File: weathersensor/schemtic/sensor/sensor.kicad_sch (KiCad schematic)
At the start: 18 parts, among them J1 Conn_Coaxial, J2 PS, J3 MS5611, J4 V_PANEL_IN, J5 V_PANEL_OUT, J6 V_BAT_IN, J7 V_BAT_OUT, U1 ESP32-DevKitC, U2 RFM95W-868S2

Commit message: Commit before fork
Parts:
- removed C1, C2: 100nF, Capacitor_THT:C_Disc_D3.0mm_W1.6mm_P2.50mm, symbol Device:C
- removed J2: PS, Connector_PinHeader_2.54mm:PinHeader_1x02_P2.54mm_Vertical, symbol Connector:Conn_01x02_Male
- removed J3: MS5611, Connector_PinHeader_2.54mm:PinHeader_1x07_P2.54mm_Vertical, symbol Connector:Conn_01x07_Female
- removed J5: V_PANEL_OUT, Connector_PinHeader_2.54mm:PinHeader_1x02_P2.54mm_Vertical, symbol Connector:Conn_01x02_Male
- removed J6: V_BAT_IN, TerminalBlock_RND:TerminalBlock_RND_205-00012_1x02_P5.00mm_Horizontal, symbol Connector:Screw_Terminal_01x02
- removed J7: V_BAT_OUT, Connector_PinHeader_2.54mm:PinHeader_1x02_P2.54mm_Vertical, symbol Connector:Conn_01x02_Male
- removed R2, R4: 510k, Resistor_THT:R_Axial_DIN0204_L3.6mm_D1.6mm_P5.08mm_Horizontal, symbol Device:R
- removed R3: 2.2M, Resistor_THT:R_Axial_DIN0204_L3.6mm_D1.6mm_P5.08mm_Horizontal, symbol Device:R
- removed U1: ESP32-DevKitC, ESP32-DEVKITC-32D:MODULE_ESP32-DEVKITC-32D, symbol Espressif:ESP32-DevKitC
- removed U2: RFM95W-868S2, RF_Module:HOPERF_RFM9XW_THT, symbol RF_Module:RFM95W-868S2
- removed U?: ESP32-WROOM, ESP32-footprints-Lib:ESP32, symbol ESP32-footprints-Shem-Lib:ESP32-WROOM
- added C3, C5, C6: 100u/16V, symbol Device:C_Polarized
- added C4: 100uF/100V, symbol Device:C_Polarized
- added J2: MS5611, Connector_PinHeader_2.54mm:PinHeader_1x07_P2.54mm_Vertical, symbol Connector:Conn_01x07_Female
- added J3: SWD, symbol Connector:Conn_01x04_Pin
- added J5: UART, symbol Connector:Conn_01x02_Pin
- added J7: BAT, Connector_JST:JST_EH_S2B-EH_1x02_P2.50mm_Horizontal, symbol Connector:Conn_01x02_Pin
- added SW1: SW_Push, symbol Switch:SW_Push
- added U1: LoRa-E5, symbol LoRa-E5:LoRa-E5
- added U2: ~, symbol tp4056_module:TP4056
- added U3: AZ1117-3.3, symbol Regulator_Linear:AZ1117-3.3
- added U4: TSR_1-2450, Converter_DCDC:Converter_DCDC_TRACO_TSR-1_THT, symbol Regulator_Switching:TSR_1-2450
- added U5: INA226, Package_SO:VSSOP-10_3x3mm_P0.5mm, symbol Sensor_Energy:INA226
- J4: value V_PANEL_IN -> PANEL
- R1: value 10M -> R; footprint Resistor_THT:R_Axial_DIN0204_L3.6mm_D1.6mm_P5.08mm_Horizontal -> (none)
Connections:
- net V_PANEL is gone; now on net GND: R1.2
- net +3.3V: now also C3.1, J2.1 (Pin_1), J3.1 (Pin_1), U1.1 (VCC), U3.2 (VO), U5.6 (VS)
- net GND: now also C3.2, C4.2, C5.2, C6.2, J2.2 (Pin_2), J3.4 (Pin_4), J7.1 (Pin_1), SW1.1, U1.14 (GND), U1.16 (GND), U1.2 (GND), U1.22 (GND), U2. (OUT), U3.1 (GND), U4.2 (GND), U5.7 (GND), U5.9 (Vin-)
- net SCL: now also J2.3 (Pin_3)
- net SDA: now also J2.4 (Pin_4)
- net at JP1.1 (A): now also J2.5 (Pin_5)
- net at R1.1: now also U2. (OUT), U5.10 (Vin+); no longer J4.1 (Pin_1)
- net RFIO: now reaches J1.1 (In)
- net RFIO: now also U1.15 (RFIO)
- new net: C6.1, U2. (OUT), U3.3 (VI)
- new net +5V: C5.1, U2. (OUT), U4.3 (Vout)
- new net BAT: J7.2 (Pin_2), U2. (OUT), U5.8 (Vbus)
- new net RST: SW1.2, U1.17 (RST)
- new net RX: J5.2 (Pin_2)
- new net SWCLK: J3.3 (Pin_3), U1.4 (PA14)
- new net SWDIO: J3.2 (Pin_2), U1.3 (PA13)
- new net TX: J5.1 (Pin_1)
- new net VD: C4.1, J4.1 (Pin_1), U4.1 (Vin)
- no-connect marks 31 -> 2
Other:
- moved on the sheet: J4

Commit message: Change to lorawan
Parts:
- U1: footprint (none) -> LoRa-E5:LoRa-E5

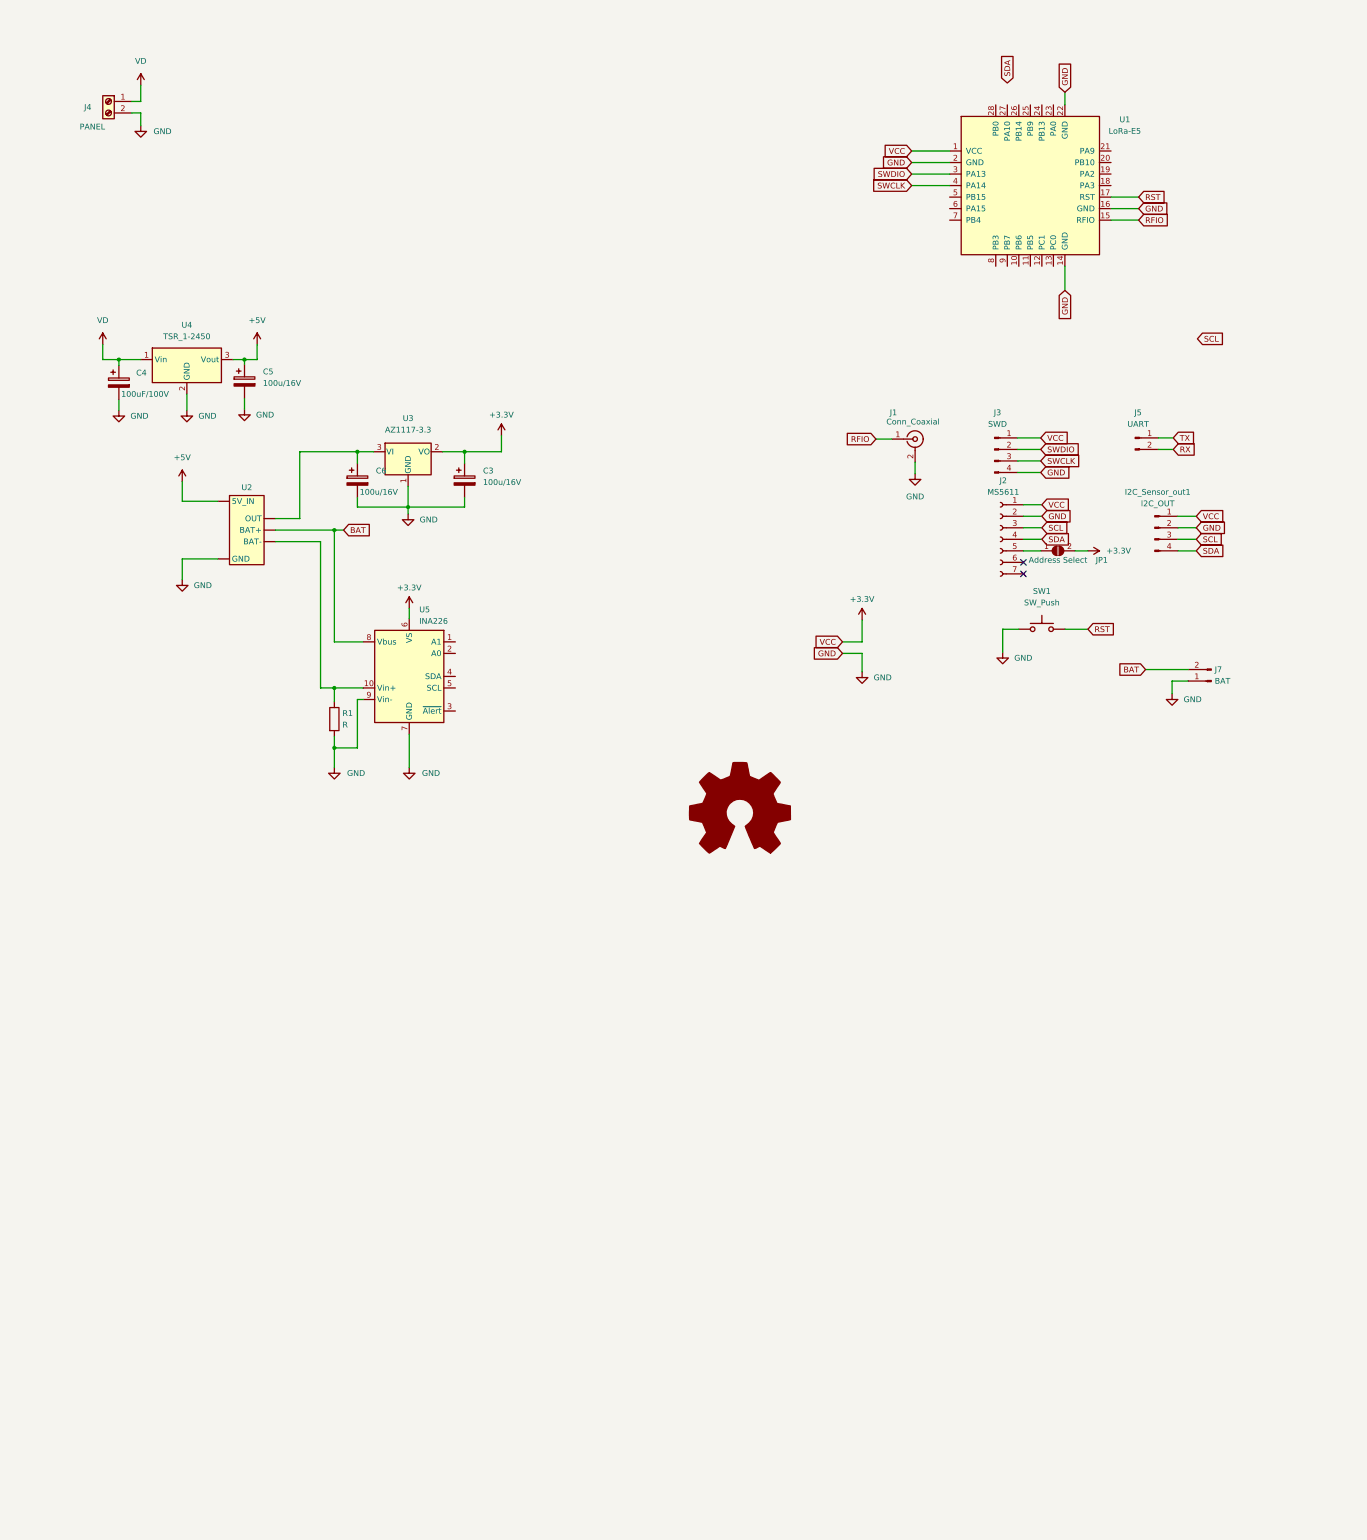
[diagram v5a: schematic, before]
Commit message: Änderung des Sensor auf neue Plattform STM32WLxx Lora-e5
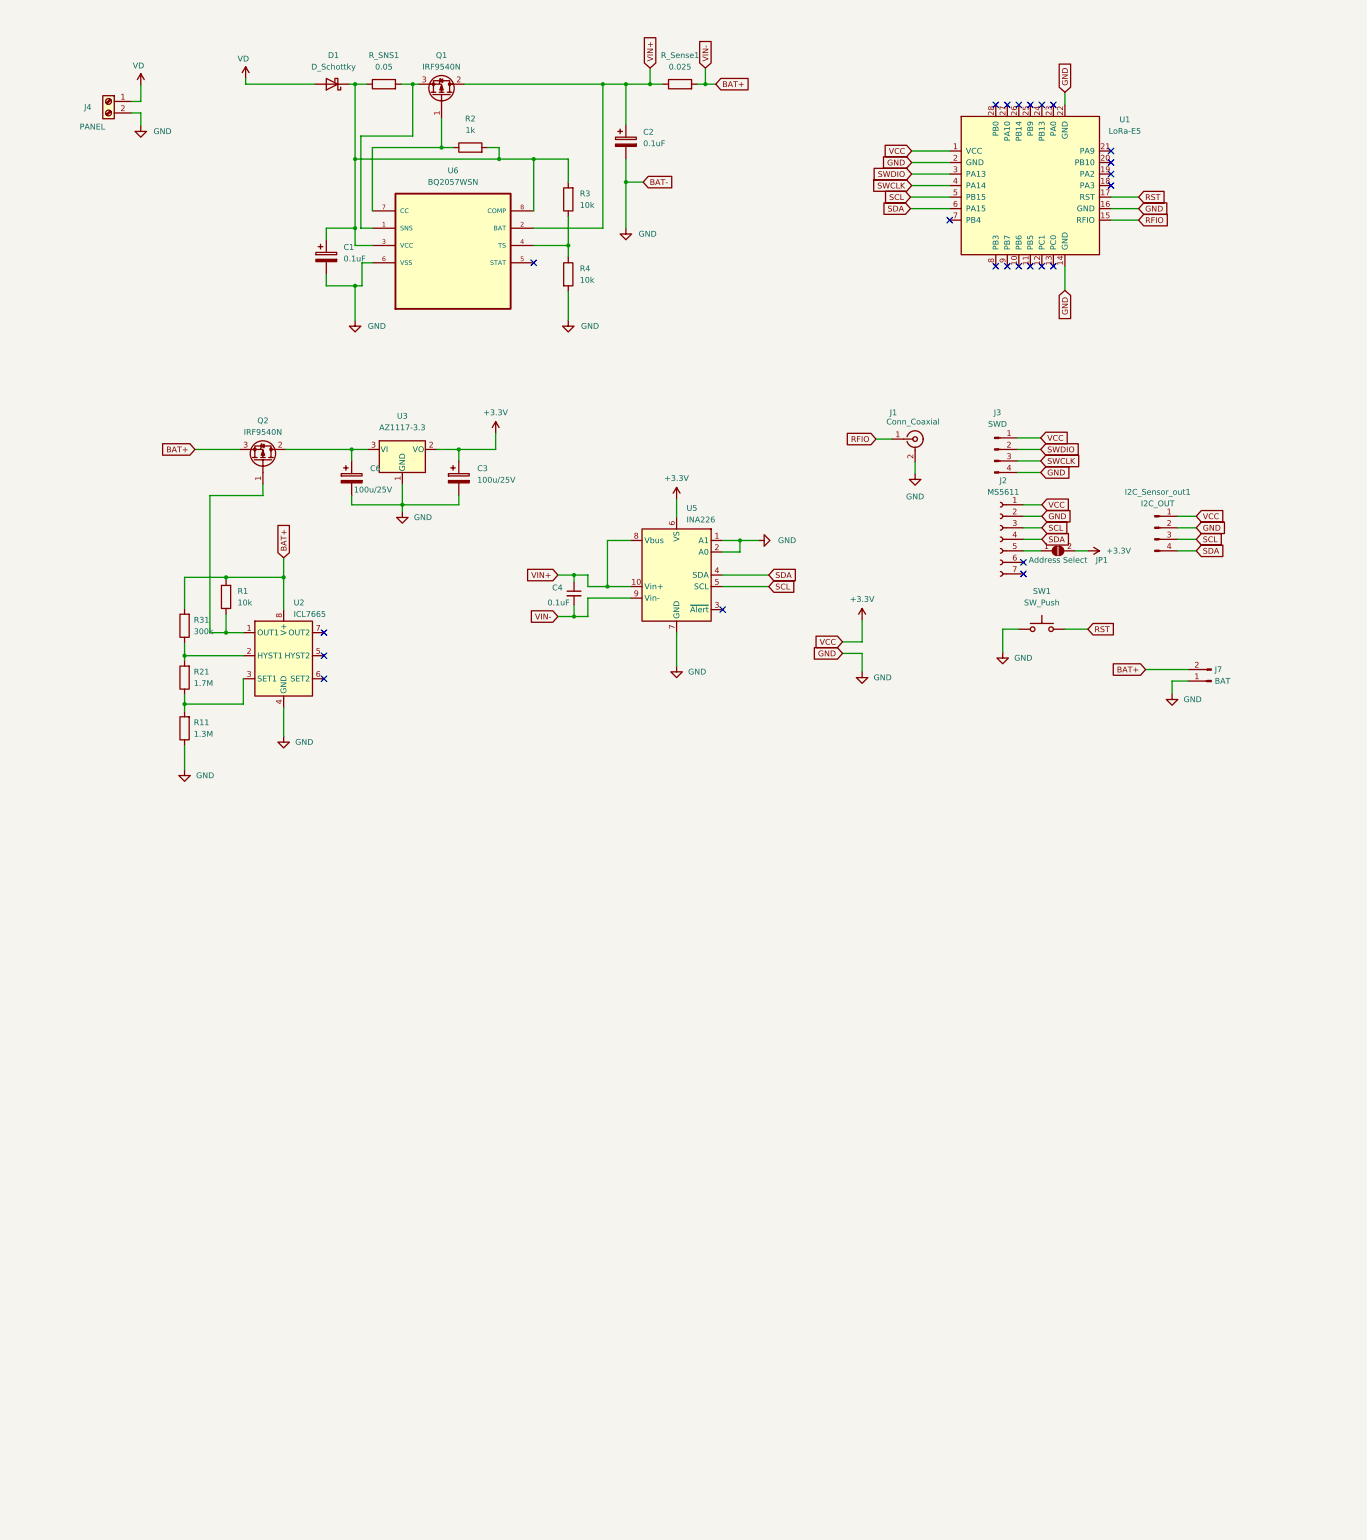
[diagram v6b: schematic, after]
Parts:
- removed C4: 100uF/100V, symbol Device:C_Polarized
- removed C5: 100u/16V, symbol Device:C_Polarized
- removed J5: UART, symbol Connector:Conn_01x02_Pin
- removed U2: ~, symbol tp4056_module:TP4056
- removed U4: TSR_1-2450, Converter_DCDC:Converter_DCDC_TRACO_TSR-1_THT, symbol Regulator_Switching:TSR_1-2450
- added C1, C2: 0.1uF, Capacitor_THT:C_Rect_L4.6mm_W2.0mm_P2.50mm_MKS02_FKP02, symbol Device:C_Polarized
- added C4: 0.1uF, Capacitor_THT:C_Rect_L4.6mm_W2.0mm_P2.50mm_MKS02_FKP02, symbol Device:C_Small
- added D1: D_Schottky, Diode_SMD:D_SOD-123, symbol Device:D_Schottky
- added Q1, Q2: IRF9540N, Package_TO_SOT_THT:TO-220-3_Horizontal_TabDown, symbol Transistor_FET:IRF9540N
- added R11: 1.3M, Resistor_THT:R_Axial_DIN0207_L6.3mm_D2.5mm_P10.16mm_Horizontal, symbol Device:R
- added R2: 1k, Resistor_THT:R_Axial_DIN0207_L6.3mm_D2.5mm_P10.16mm_Horizontal, symbol Device:R
- added R21: 1.7M, Resistor_THT:R_Axial_DIN0207_L6.3mm_D2.5mm_P10.16mm_Horizontal, symbol Device:R
- added R3, R4: 10k, Resistor_THT:R_Axial_DIN0207_L6.3mm_D2.5mm_P10.16mm_Horizontal, symbol Device:R
- added R31: 300k, Resistor_THT:R_Axial_DIN0207_L6.3mm_D2.5mm_P10.16mm_Horizontal, symbol Device:R
- added R_SNS1: 0.05, Resistor_SMD:R_2512_6332Metric, symbol Device:R
- added R_Sense1: 0.025, Resistor_SMD:R_2512_6332Metric, symbol Device:R
- added U2: ICL7665, Package_DIP:DIP-8_W7.62mm_LongPads, symbol icl7665:ICL7665
- added U6: BQ2057WSN, BQ2057WSN:SOIC127P599X175-8N, symbol BQ2057WSN:BQ2057WSN
- C3, C6: value 100u/16V -> 100u/25V; footprint (none) -> Capacitor_THT:CP_Radial_D5.0mm_P2.50mm
- J3: footprint (none) -> Connector_JST:JST_XH_B4B-XH-AM_1x04_P2.50mm_Vertical
- R1: value R -> 10k; footprint (none) -> Resistor_THT:R_Axial_DIN0207_L6.3mm_D2.5mm_P10.16mm_Horizontal
- SW1: footprint (none) -> Button_Switch_SMD:SW_SPST_CK_RS282G05A3
- U3: footprint (none) -> Package_TO_SOT_SMD:SOT-223
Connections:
- net GND: now also U5.1 (A1), U5.2 (A0), C1.2, C2.2, R11.1, R4.2, U2.4 (GND), U6.6 (VSS); no longer R1.2, U5.9 (Vin-)
- net SCL: now also U1.5 (PB15), U5.5 (SCL)
- net SDA: now also U1.6 (PA15), U5.4 (SDA)
- net VD: now also D1.2 (A)
- net at C6.1, U3.3 (VI): now also Q2.2 (D)
- net at R1.1: now also Q2.1 (G), U2.1 (OUT1); no longer U5.10 (Vin+)
- net BAT renamed BAT+
- net BAT+: now also R1.2, U5.9 (Vin-), C4.2, Q2.3 (S), R31.2, R_Sense1.2, U2.8 (V+); no longer U5.8 (Vbus)
- new net: R3.1, R4.1, U6.4 (TS)
- new net: Q1.1 (G), R2.1, U6.7 (CC)
- new net: C1.1, D1.1 (K), R2.2, R3.2, R_SNS1.1, U6.3 (VCC), U6.8 (COMP)
- new net: R11.2, R21.1, U2.3 (SET1)
- new net: R21.2, R31.1, U2.2 (HYST1)
- new net: Q1.3 (S), R_SNS1.2, U6.1 (SNS)
- new net VIN+: C2.1, C4.1, Q1.2 (D), R_Sense1.1, U5.10 (Vin+), U5.8 (Vbus), U6.2 (BAT)
- no-connect marks 2 -> 24
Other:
- moved on the sheet: C3, C6, U3, U5
